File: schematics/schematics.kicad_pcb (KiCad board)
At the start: 2 copper layers, 17.5 x 44.3 mm, 8 parts, among them J1 Conn_01x02, J2 Conn_01x07_Female, U1 ATmega8A-PU, U2 AMS1117-3.3, U3 NRF24L01_Breakout

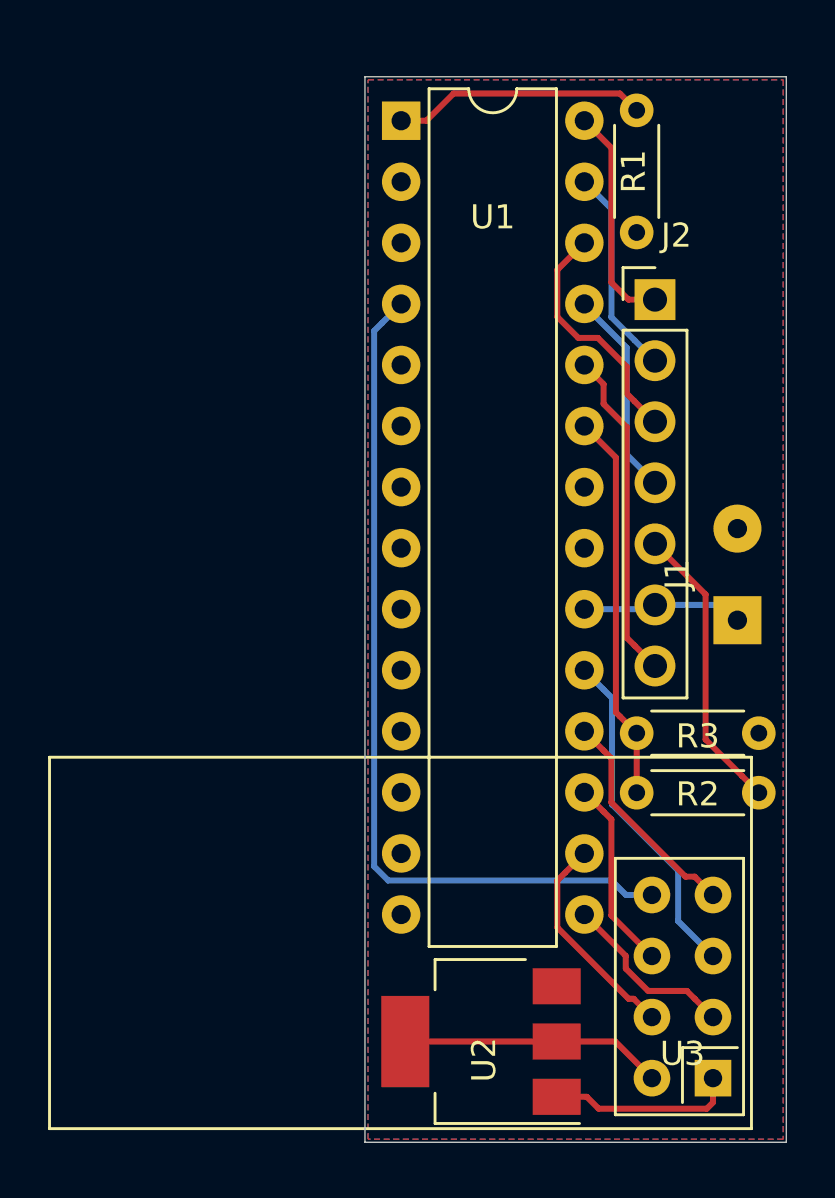
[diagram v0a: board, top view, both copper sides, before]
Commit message: Measuring the battery voltage using the internal bandgap voltage input (1.3V), removing the voltage divider
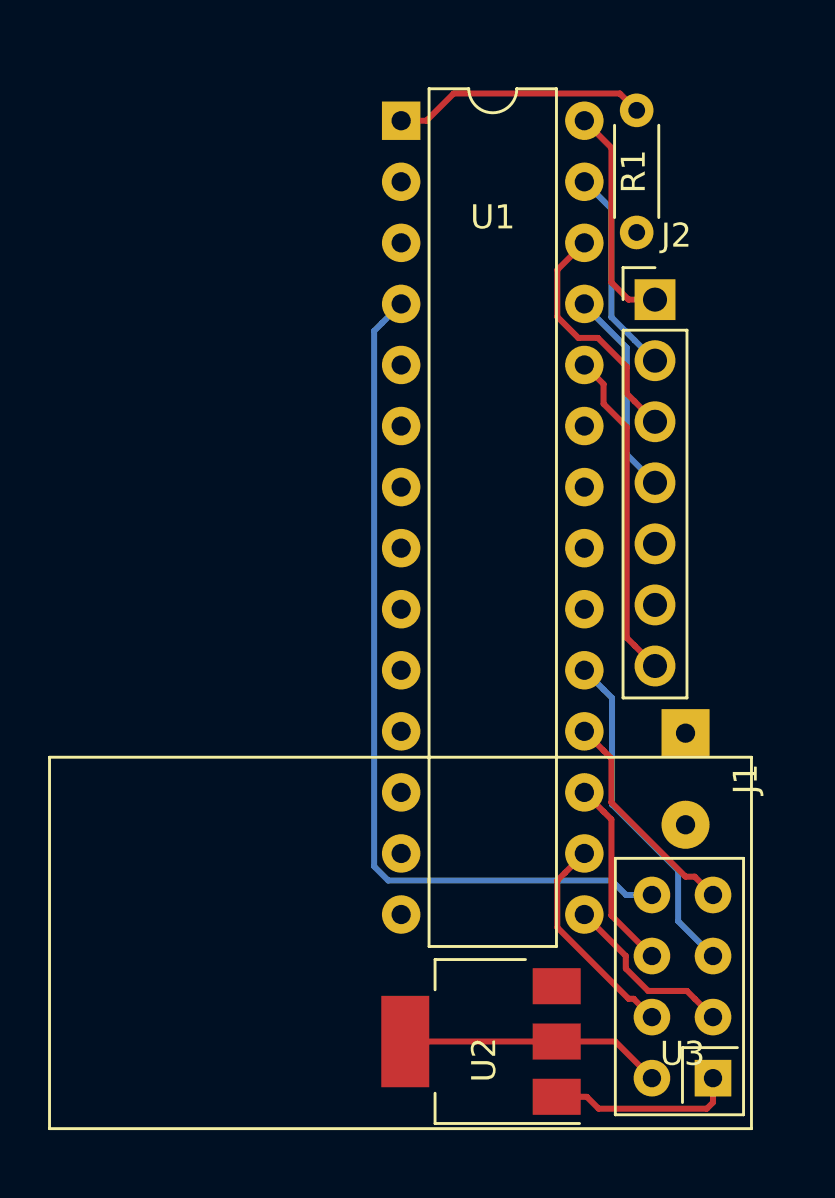
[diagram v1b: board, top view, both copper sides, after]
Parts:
- removed R2, R3: 220k, Resistor_THT:R_Axial_DIN0204_L3.6mm_D1.6mm_P5.08mm_Horizontal
- moved J1 5.17 mm to (142.7, 101.1), turned to 270 degrees
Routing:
- net /ADC_IN: track 16.2 -> 0.00 mm
- net /GND: track 20.0 -> 7.83 mm
- net /BATTERY_IN: track 6.70 -> 0.00 mm
- removed copper zone on F.Cu, net /BATTERY_IN
- removed copper zone on B.Cu, net /GND
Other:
- board outline removed

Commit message: Updated PCB.
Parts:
- J1: value Conn_01x02 -> POWER; footprint Connector_Wire:SolderWirePad_1x02_P3.81mm_Drill0.8mm -> Connector_PinHeader_2.00mm:PinHeader_1x02_P2.00mm_Vertical
- J2: value Conn_01x07_Female -> PSX_CONNECTOR
- U3: value NRF24L01_Breakout -> NRF24L01_BREAKOUT
- moved J1 1.44 mm to (143.8, 102.1), turned to 0 degrees
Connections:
- net /ADC_IN renamed Net-(U1-Pad23)
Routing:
- added copper zone on F.Cu, net /BATTERY_IN
- added copper zone on B.Cu, net /GND
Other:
- board outline added: 17.8 x 45.7 mm
- board text added: "Atmega8a-PU"
- board text added: "GND"
- board text added: "PSX_ACK"
- board text added: "PSX_ATT"
- board text added: "PSX_CLK"
- board text added: "PSX_CMD"
- board text added: "PSX_DATA"
- board text added: "VCC"
- board text added: "Vcc"
